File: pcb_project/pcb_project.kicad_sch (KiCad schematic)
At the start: 15 parts, among them J1 Conn_01x10_Pin

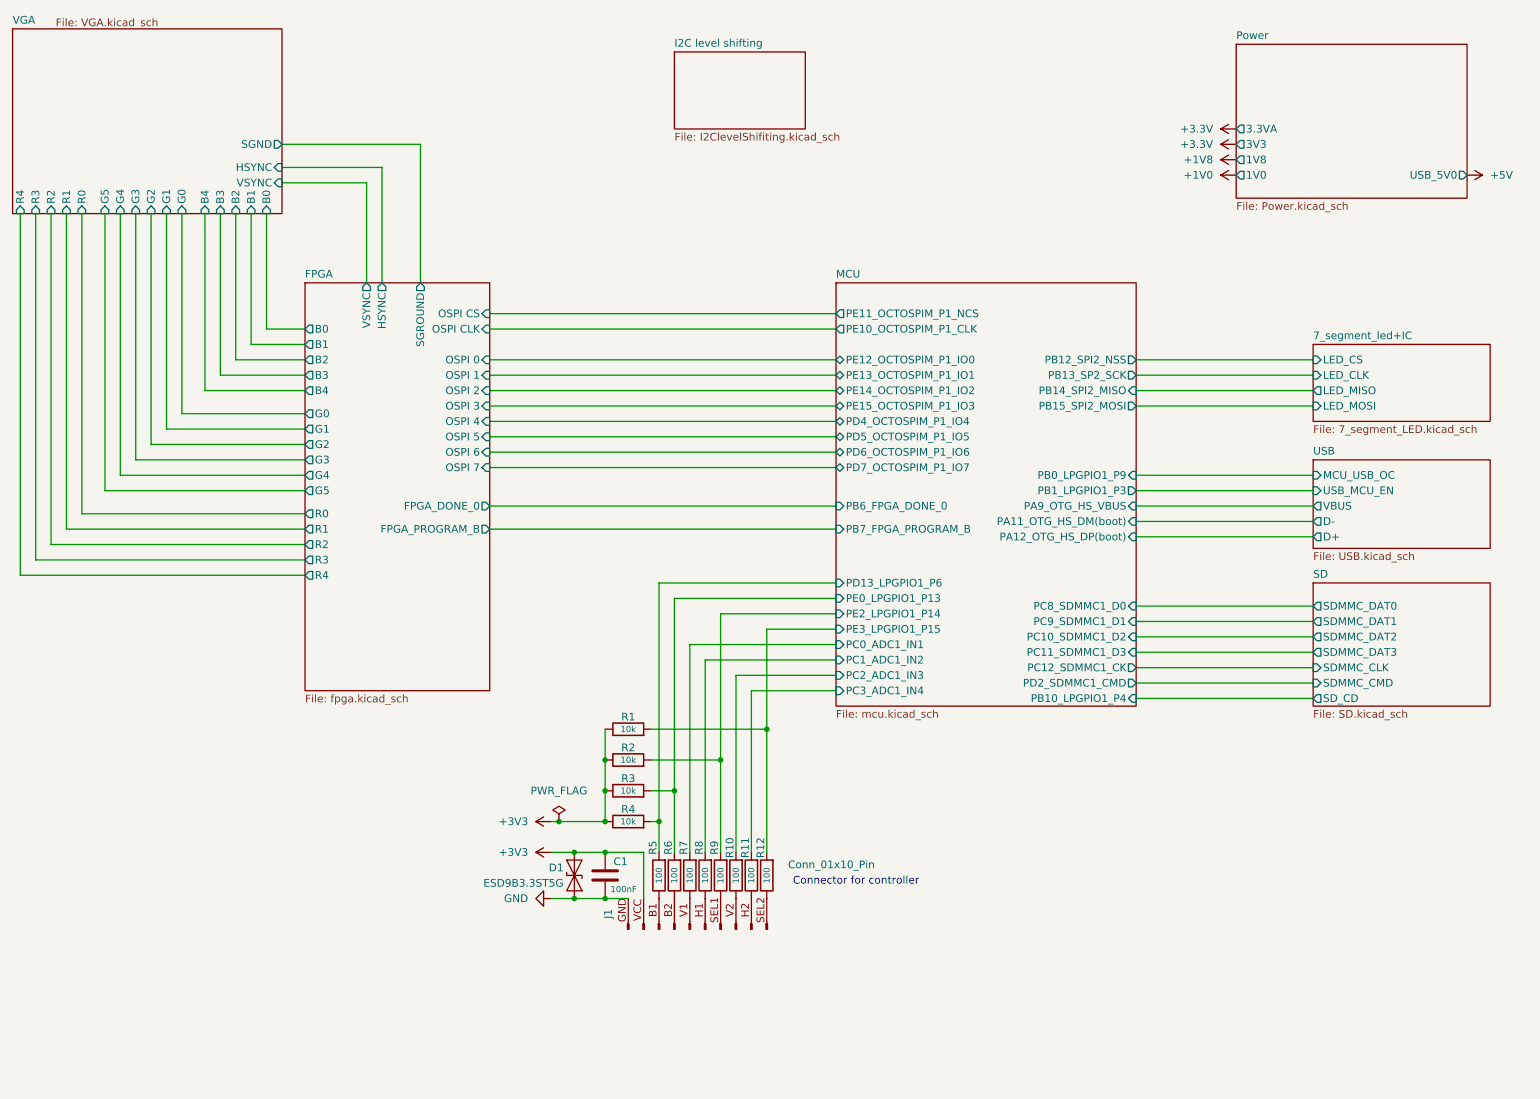
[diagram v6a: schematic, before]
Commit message: Fix ERC errors and update PCB from schematic
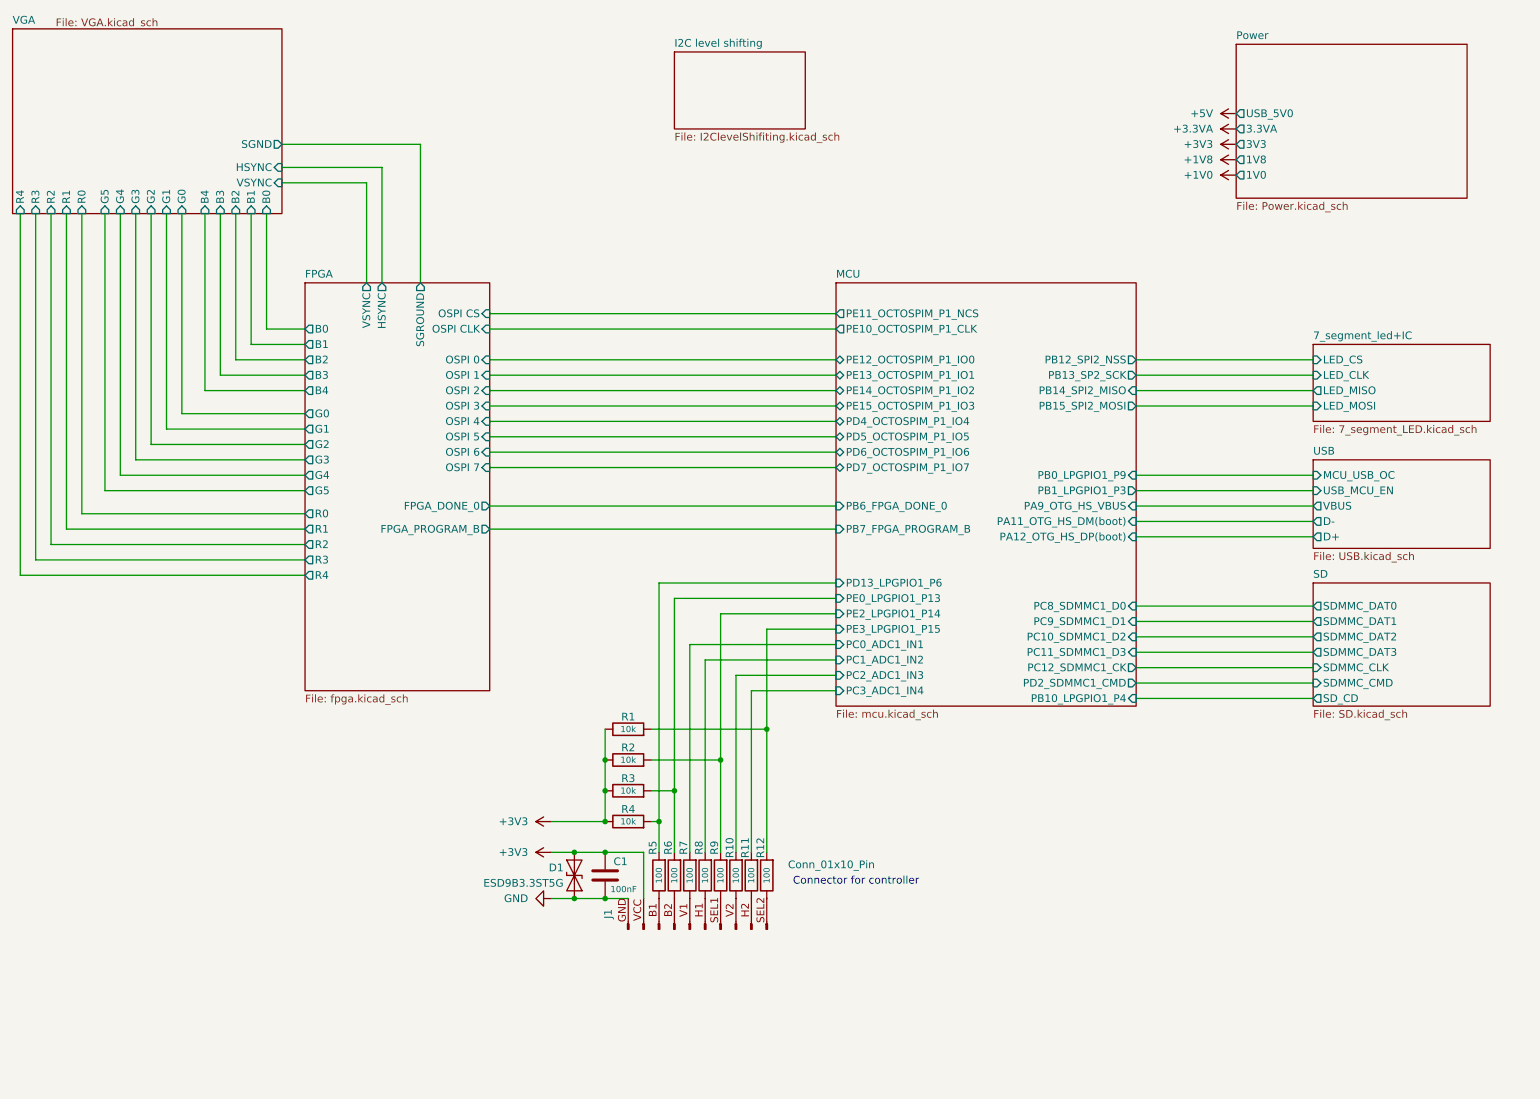
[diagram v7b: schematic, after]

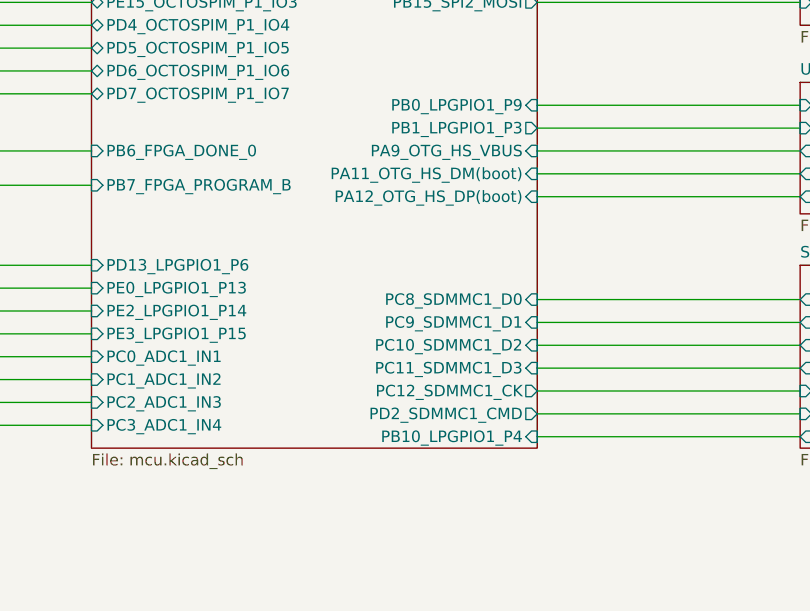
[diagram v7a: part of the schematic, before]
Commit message: Minor schematic changes for easier Layout
- Proper TVS symbol for MicroSD
- Rename USB data lines net name to allow for differential routing
- Change SDMMC_CD GPIO to easier MCU pin
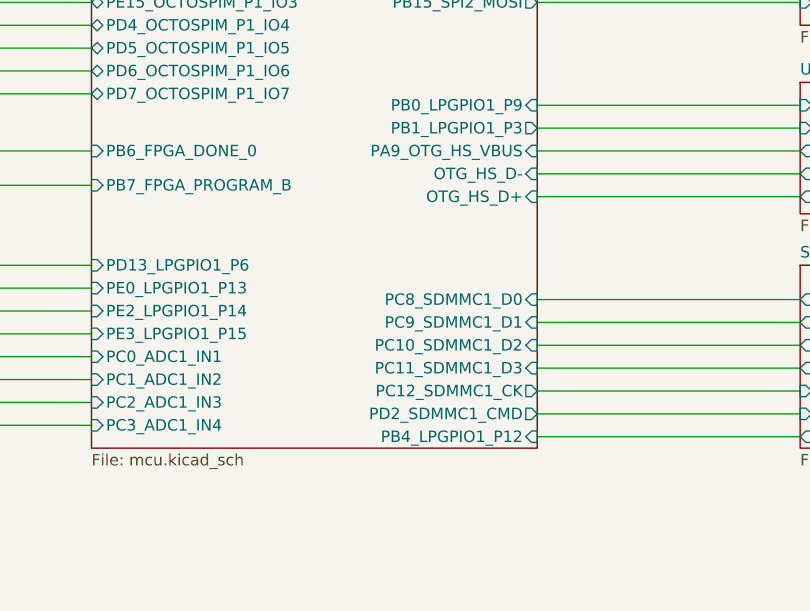
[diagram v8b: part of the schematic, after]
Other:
- sheet MCU ports: added OTG_HS_D+, OTG_HS_D-, PB4_LPGPIO1_P12; removed PA11_OTG_HS_DM(boot), PA12_OTG_HS_DP(boot), PB10_LPGPIO1_P4
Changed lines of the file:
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@@
-			)
-		)
-		(pin "PB10_LPGPIO1_P4" input
-			(at 210.82 133.35 0)
-			(effects
-				(font
-					(size 1.27 1.27)
-				)
-				(justify right)
 			)
 		)
@@
 			)
 		)
-		(pin "PA11_OTG_HS_DM(boot)" input
-			(at 210.82 104.14 0)
-			(effects
-				(font
-					(size 1.27 1.27)
-				)
-				(justify right)
-			)
-		)
-		(pin "PA12_OTG_HS_DP(boot)" input
-			(at 210.82 106.68 0)
-			(effects
-				(font
-					(size 1.27 1.27)
-				)
-				(justify right)
-			)
-		)
 		(pin "PB13_SP2_SCK" output
 			(at 210.82 80.01 0)
@@
 			)
 		)
+		(pin "OTG_HS_D+" input
+			(at 210.82 106.68 0)
+			(effects
+				(font
+					(size 1.27 1.27)
+				)
+				(justify right)
+			)
+		)
+		(pin "OTG_HS_D-" input
+			(at 210.82 104.14 0)
+			(effects
+				(font
+					(size 1.27 1.27)
+				)
+				(justify right)
+			)
+		)
+		(pin "PB4_LPGPIO1_P12" input
+			(at 210.82 133.35 0)
+			(effects
+				(font
+					(size 1.27 1.27)
+				)
+				(justify right)
+			)
+		)
